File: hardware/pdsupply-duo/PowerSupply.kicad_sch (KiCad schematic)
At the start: 4 parts

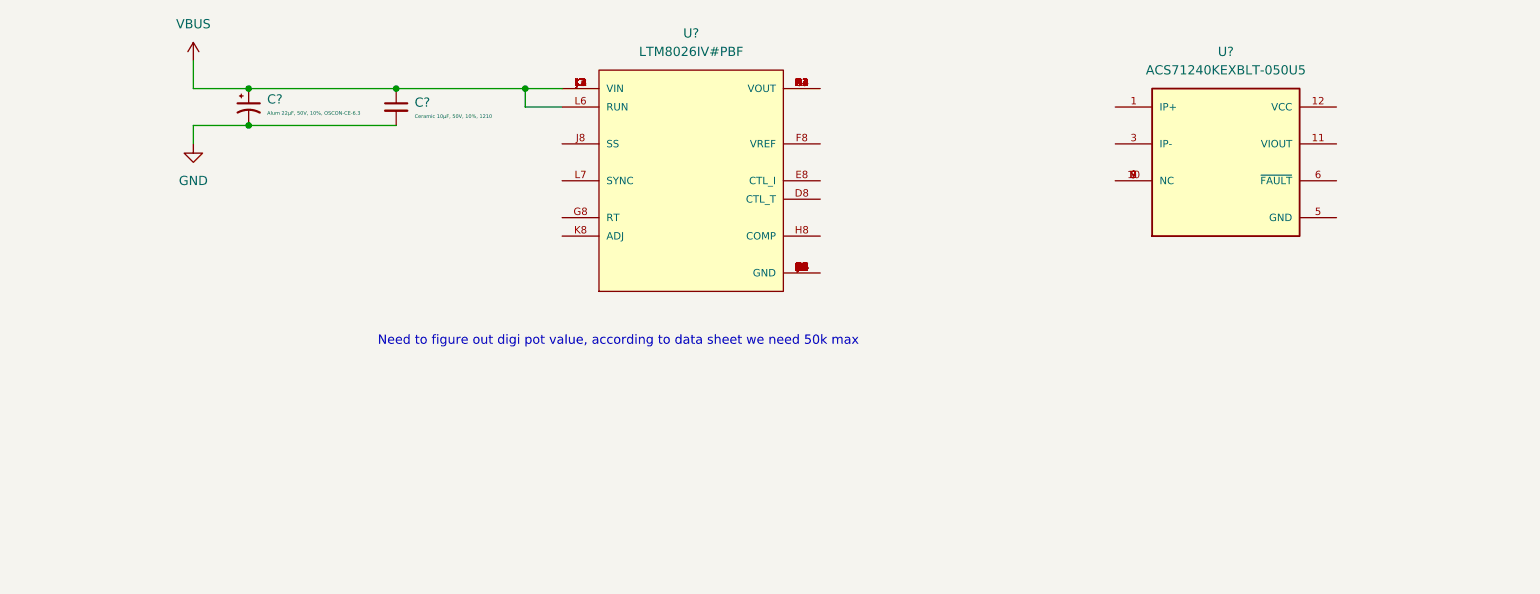
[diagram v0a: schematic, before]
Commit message: Added usb PD interface
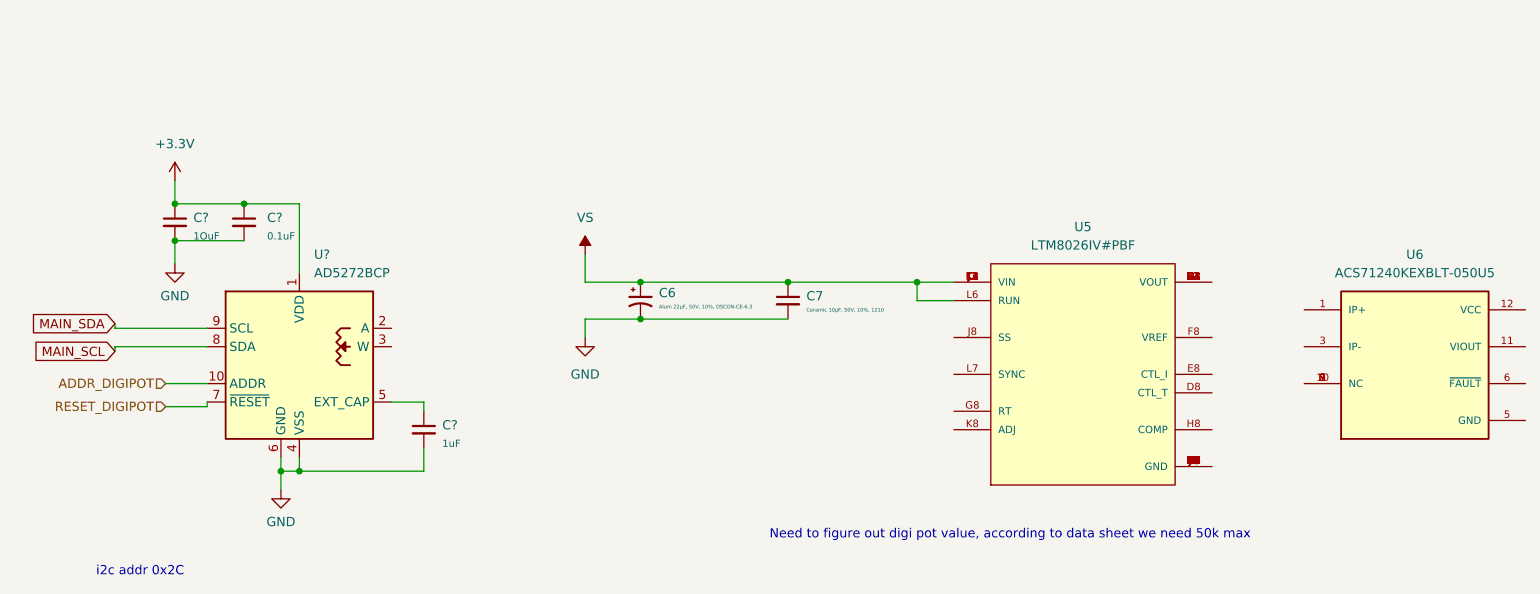
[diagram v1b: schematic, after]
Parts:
- added C?: 1uF, symbol Device:C_Small
- added C?: 0.1uF, symbol Device:C_Small
- added C?: 1OuF, symbol Device:C_Small
- added U?: AD5272BCP, Package_CSP:LFCSP-WD-10-1EP_3x3mm_P0.5mm_EP1.64x2.38mm, symbol Potentiometer_Digital:AD5272BCP
- gave numbers to parts that had none: 4
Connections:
- net GND: now also C?.2, C?.2, C?.2, U?.11 (VSS), U?.4 (VSS), U?.6 (GND)
- net VBUS renamed VS
- new net: C?.1, U?.5 (EXT_CAP)
- new net +3V3: C?.1, C?.1, U?.1 (VDD)
- new net ADDR_DIGIPOT: U?.10 (ADDR)
- new net MAIN_SCL: U?.8 (SDA)
- new net MAIN_SDA: U?.9 (SCL)
- new net RESET_DIGIPOT: U?.7 (~{RESET})
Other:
- note added: "i2c addr 0x2C"
- moved on the sheet: C6, C7, U5, U6

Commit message: SCH 85% done
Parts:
- added C?: .1uF, symbol Device:C_Small
- added C?: 22µF, 25V, 1210, symbol Device:C_Small
- added C?: Decide, symbol Device:C_Small
- added C?: 47µF, 20V, 45mΩ, OS-CON, 20SVPS47M, symbol Device:C_Polarized_US
- added JP?: Jumper_2_Open, symbol Jumper:Jumper_2_Open
- added R?: 4k, symbol Device:R_Small_US
- added R?: decide, symbol Device:R_Small_US
- added R?: 510k, symbol Device:R_Small_US
- renumbered C7 to C?, C6 to C?, U6 to U?, U5 to U?
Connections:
- net +3V3: now also U?.12 (VCC), C?.1
- net GND: now also U?.5 (GND), U?.A5 (GND), U?.A6 (GND), U?.A7 (GND), U?.A8 (GND), U?.B5 (GND), U?.B6 (GND), U?.B7 (GND), U?.B8 (GND), U?.C5 (GND), U?.C6 (GND), U?.C7 (GND), U?.C8 (GND), U?.D5 (GND), U?.D6 (GND), U?.D7 (GND), U?.E1 (GND), U?.E2 (GND), U?.E3 (GND), U?.E4 (GND), U?.E5 (GND), U?.E6 (GND), U?.E7 (GND), U?.F1 (GND), U?.F2 (GND), U?.F3 (GND), U?.F4 (GND), U?.F5 (GND), U?.F6 (GND), U?.F7 (GND), U?.G1 (GND), U?.G2 (GND), U?.G3 (GND), U?.G4 (GND), U?.G5 (GND), U?.G6 (GND), U?.G7 (GND), U?.H5 (GND), U?.H6 (GND), U?.H7 (GND), U?.J5 (GND), U?.J6 (GND), U?.J7 (GND), U?.K5 (GND), U?.K6 (GND), U?.K7 (GND), U?.L5 (GND), U?.L8 (GND), C?.2, C?.2, C?.2, C?.2, JP?.1 (A), R?.1
- net VS: now also R?.1; no longer U?.L6 (RUN)
- net at U?.1 (IP+): now also U?.A1 (VOUT), U?.A2 (VOUT), U?.A3 (VOUT), U?.A4 (VOUT), U?.B1 (VOUT), U?.B2 (VOUT), U?.B3 (VOUT), U?.B4 (VOUT), U?.C1 (VOUT), U?.C2 (VOUT), U?.C3 (VOUT), U?.C4 (VOUT), U?.D1 (VOUT), U?.D2 (VOUT), U?.D3 (VOUT), U?.D4 (VOUT), C?.1, C?.1
- net Isense: now reaches U?.11 (VIOUT)
- net Isense: now also C?.1
- net Vout: now reaches U?.3 (IP-)
- net at U?.D8 (CTL_T): now also U?.E8 (CTL_I), U?.F8 (VREF)
- net at U?.G8 (RT): now also R?.2
- net Radj: now reaches U?.K8 (ADJ)
- net Radj: now also U?.2 (A), R?.1
- net SYNC: now reaches U?.L7 (SYNC)
- net SYNC: now also JP?.2 (B)
- net at U?.3 (W): now also R?.2
- new net: R?.2, U?.L6 (RUN)
- no-connect marks 0 -> 4
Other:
- note added: "When using the SYNC function, apply a resistor value equivalent to 20% lower than the SYNC pulse frequency"
- note removed: "Need to figure out digi pot value, according to data sheet we need 50k max"
- note removed: "i2c addr 0x2C"
- moved on the sheet: C?, U?
